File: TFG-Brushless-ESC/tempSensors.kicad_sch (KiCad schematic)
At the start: 18 parts

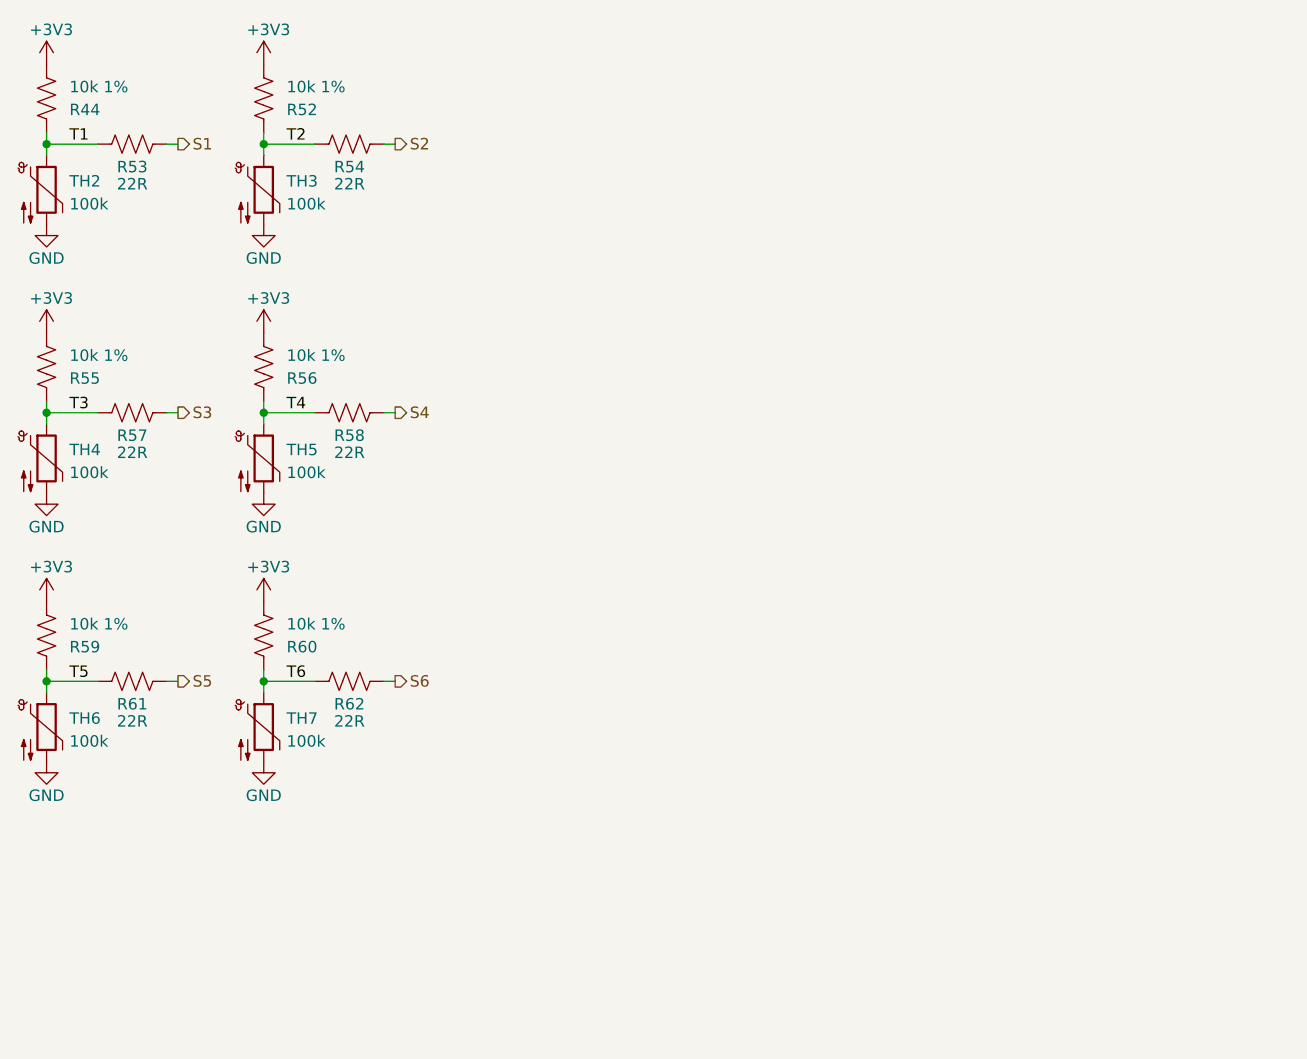
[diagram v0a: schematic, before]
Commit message: Traducción nombres
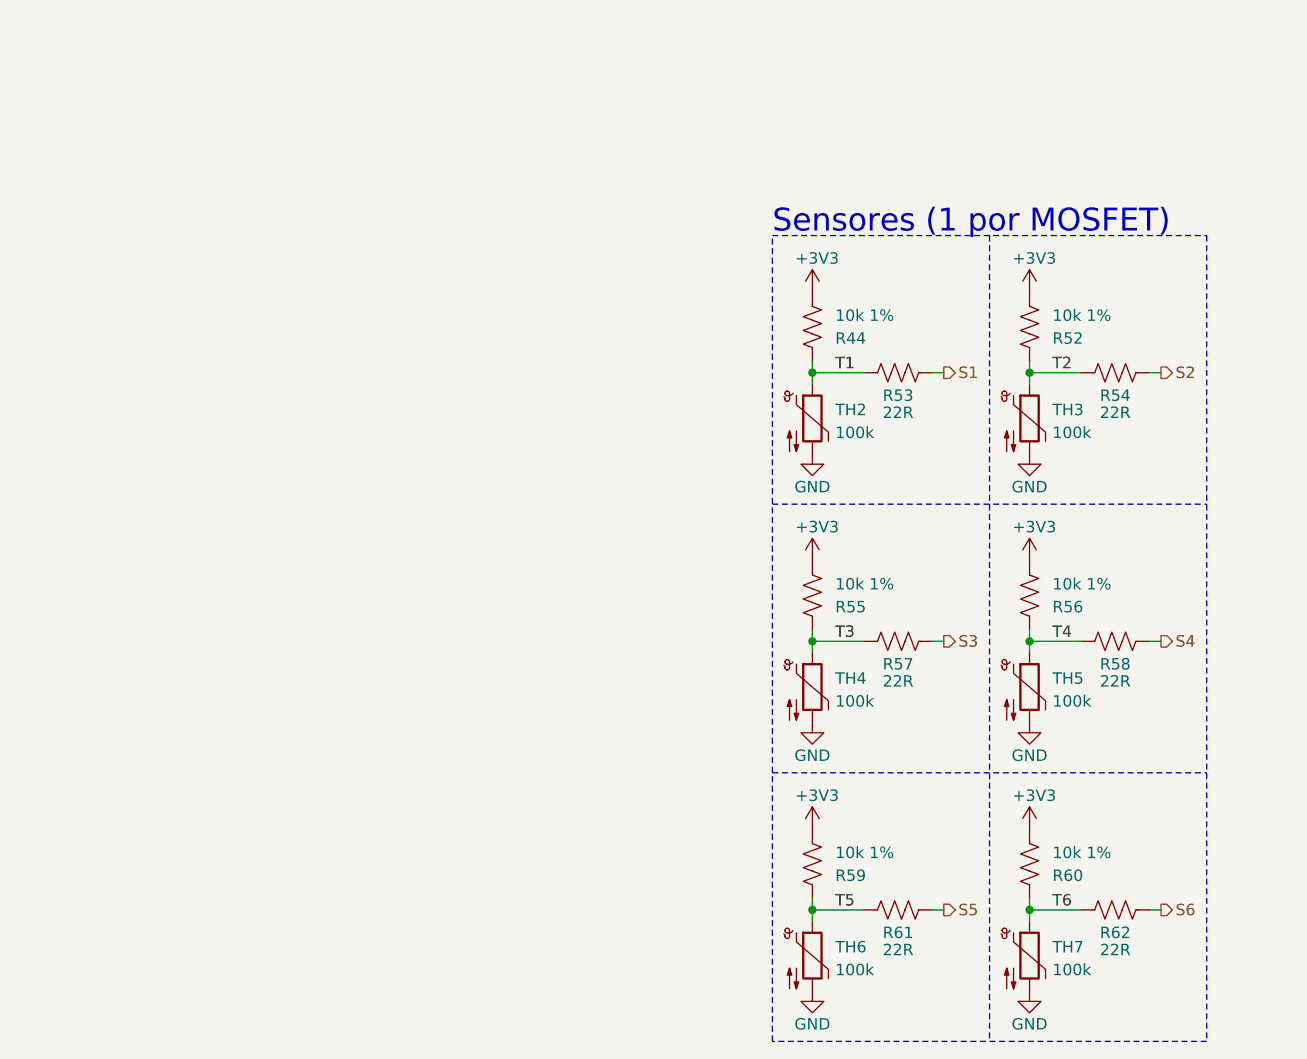
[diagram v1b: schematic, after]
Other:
- note added: "Sensores (1 por MOSFET)"
- moved on the sheet: R44, R52, R53, R54, R55, R56, R57, R58, R59, R60, R61, R62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
